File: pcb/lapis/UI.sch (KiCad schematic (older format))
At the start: 15 parts, among them J10 Conn_01x04, Q6 MMBF0201NLT1G

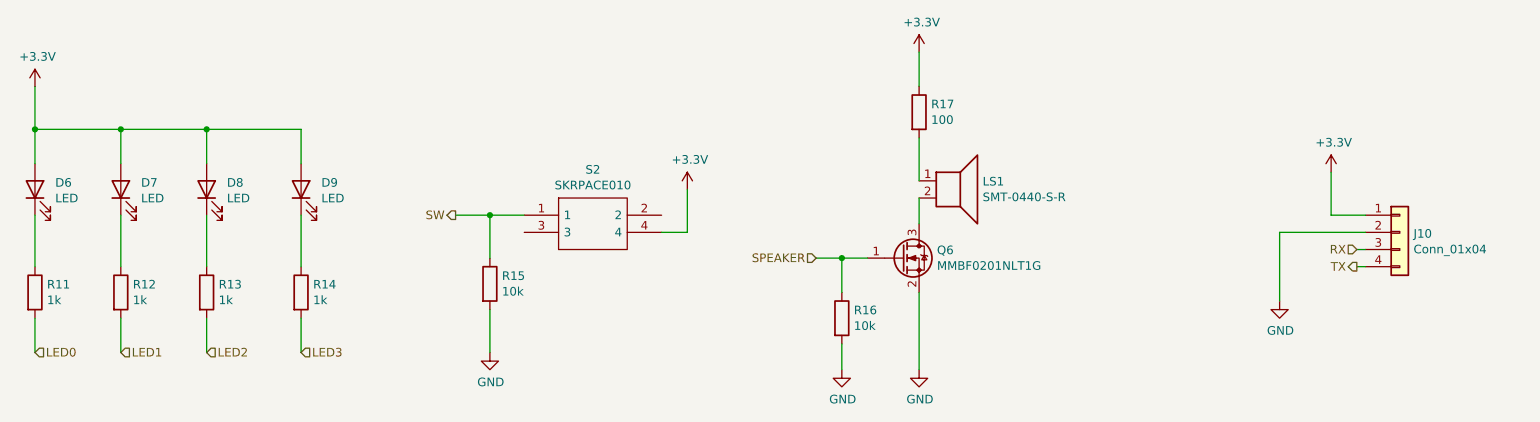
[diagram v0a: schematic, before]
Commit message: 信地旋回探索
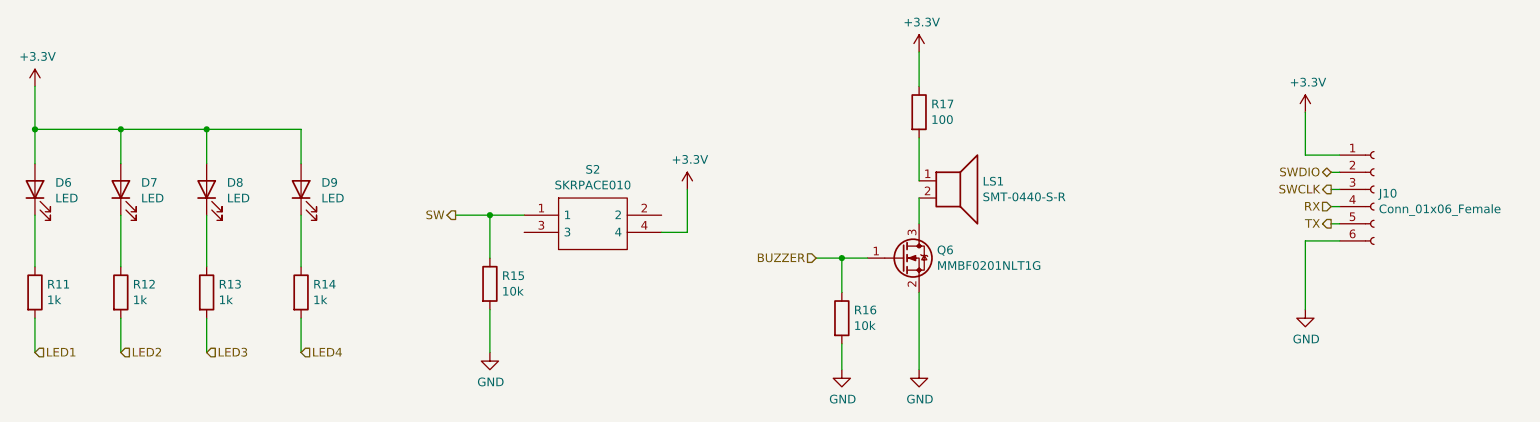
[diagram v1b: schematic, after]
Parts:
- removed J10: Conn_01x04, Connector_PinSocket_2.54mm:PinSocket_1x04_P2.54mm_Vertical, symbol Connector_Generic:Conn_01x04
- added J10: Conn_01x06_Female, Connector_PinHeader_1.27mm:PinHeader_1x06_P1.27mm_Vertical, symbol Connector:Conn_01x06_Female
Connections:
- net LED0 is gone; now on net LED1: R11.2
- net +3V3: now also J10.1 (Pin_1)
- net GND: now also J10.6 (Pin_6)
- net LED1: no longer R12.2
- net LED2: now also R12.2; no longer R13.2
- net LED3: now also R13.2; no longer R14.2
- net RX: now also J10.4 (Pin_4)
- net TX: now also J10.5 (Pin_5)
- net SPEAKER renamed BUZZER
- new net LED4: R14.2
- new net SWCLK: J10.3 (Pin_3)
- new net SWDIO: J10.2 (Pin_2)
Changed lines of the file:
@@
 $Descr A4 11693 8268
 encoding utf-8
-Sheet 14 14
+Sheet 7 15
 Title ""
 Date ""
@@
 Connection ~ 4500 3300
 $Comp
-L power:+3.3V #PWR?
-U 1 1 603B98FF
-P 9400 3050
-AR Path="/5FA81D59/603B98FF" Ref="#PWR?"  Part="1"
-AR Path="/603AF16B/603B98FF" Ref="#PWR0165"  Part="1"
-F 0 "#PWR0165" H 9400 2900 50  0001 C CNN
-F 1 "+3.3V" H 9415 3223 50  0000 C CNN
-F 2 "" H 9400 3050 50  0001 C CNN
-F 3 "" H 9400 3050 50  0001 C CNN
-	1    9400 3050
-	1    0    0    -1
-$EndComp
-$Comp
-L power:GND #PWR?
-U 1 1 603B9905
-P 9100 3800
-AR Path="/5FA81D59/603B9905" Ref="#PWR?"  Part="1"
-AR Path="/603AF16B/603B9905" Ref="#PWR0166"  Part="1"
-F 0 "#PWR0166" H 9100 3550 50  0001 C CNN
-F 1 "GND" H 9105 3627 50  0000 C CNN
-F 2 "" H 9100 3800 50  0001 C CNN
-F 3 "" H 9100 3800 50  0001 C CNN
-	1    9100 3800
-	1    0    0    -1
-$EndComp
-$Comp
-L Connector_Generic:Conn_01x04 J?
-U 1 1 603B990B
-P 9800 3400
-AR Path="/5FA81D59/603B990B" Ref="J?"  Part="1"
-AR Path="/603AF16B/603B990B" Ref="J10"  Part="1"
-F 0 "J10" H 9880 3392 50  0000 L CNN
-F 1 "Conn_01x04" H 9880 3301 50  0000 L CNN
-F 2 "Connector_PinSocket_2.54mm:PinSocket_1x04_P2.54mm_Vertical" H 9800 3400 50  0001 C CNN
-F 3 "~" H 9800 3400 50  0001 C CNN
-	1    9800 3400
-	1    0    0    -1
-$EndComp
-Wire Wire Line
-	9400 3050 9400 3300
-Wire Wire Line
-	9400 3300 9600 3300
-Wire Wire Line
-	9100 3400 9100 3800
-Wire Wire Line
-	9100 3400 9600 3400
-Wire Wire Line
-	9600 3500 9550 3500
-Wire Wire Line
-	9600 3600 9550 3600
-$Comp
 L Device:Speaker LS?
 U 1 1 603B9919
@@
 	7000 3750 7000 4200
 Text HLabel 6400 3550 0    50   Input ~ 0
-SPEAKER
+BUZZER
 $Comp
 L Device:R R?
@@
 	4500 3300 4700 3300
 Text HLabel 3400 4100 2    50   Input ~ 0
+LED4
+Text HLabel 2850 4100 2    50   Input ~ 0
 LED3
-Text HLabel 2850 4100 2    50   Input ~ 0
+Text HLabel 2350 4100 2    50   Input ~ 0
 LED2
-Text HLabel 2350 4100 2    50   Input ~ 0
+Text HLabel 1850 4100 2    50   Input ~ 0
 LED1
-Text HLabel 1850 4100 2    50   Input ~ 0
-LED0
-Text HLabel 9550 3500 0    50   Input ~ 0
-RX
-Text HLabel 9550 3600 0    50   Output ~ 0
-TX
 $Comp
 L power:+3.3V #PWR?
@@
 Wire Wire Line
 	5650 3150 5650 3400
+Wire Wire Line
+	9450 3250 9400 3250
+Wire Wire Line
+	9450 3350 9400 3350
+Text HLabel 9400 3250 0    50   Input ~ 0
+RX
+Text HLabel 9400 3350 0    50   Output ~ 0
+TX
+$Comp
+L Connector:Conn_01x06_Female J10
+U 1 1 61A6FAA6
+P 9650 3150
+F 0 "J10" H 9678 3126 50  0000 L CNN
+F 1 "Conn_01x06_Female" H 9678 3035 50  0000 L CNN
+F 2 "Connector_PinHeader_1.27mm:PinHeader_1x06_P1.27mm_Vertical" H 9650 3150 50  0001 C CNN
+F 3 "~" H 9650 3150 50  0001 C CNN
+	1    9650 3150
+	1    0    0    -1
+$EndComp
+Wire Wire Line
+	9450 3050 9400 3050
+Wire Wire Line
+	9450 3150 9400 3150
+Text HLabel 9400 3050 0    50   BiDi ~ 0
+SWDIO
+Text HLabel 9400 3150 0    50   Output ~ 0
+SWCLK
+Wire Wire Line
+	9250 3450 9450 3450
+Wire Wire Line
+	9250 2950 9450 2950
+Wire Wire Line
+	9250 2700 9250 2950
+Wire Wire Line
+	9250 3450 9250 3850
+$Comp
+L power:+3.3V #PWR?
+U 1 1 603B98FF
+P 9250 2700
+AR Path="/5FA81D59/603B98FF" Ref="#PWR?"  Part="1"
+AR Path="/603AF16B/603B98FF" Ref="#PWR0165"  Part="1"
+F 0 "#PWR0165" H 9250 2550 50  0001 C CNN
+F 1 "+3.3V" H 9265 2873 50  0000 C CNN
+F 2 "" H 9250 2700 50  0001 C CNN
+F 3 "" H 9250 2700 50  0001 C CNN
+	1    9250 2700
+	1    0    0    -1
+$EndComp
+$Comp
+L power:GND #PWR?
+U 1 1 603B9905
+P 9250 3850
+AR Path="/5FA81D59/603B9905" Ref="#PWR?"  Part="1"
+AR Path="/603AF16B/603B9905" Ref="#PWR0166"  Part="1"
+F 0 "#PWR0166" H 9250 3600 50  0001 C CNN
+F 1 "GND" H 9255 3677 50  0000 C CNN
+F 2 "" H 9250 3850 50  0001 C CNN
+F 3 "" H 9250 3850 50  0001 C CNN
+	1    9250 3850
+	1    0    0    -1
+$EndComp
 $EndSCHEMATC
